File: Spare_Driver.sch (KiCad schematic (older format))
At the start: 48 parts, among them J12 CHECK FOOTPRINT, J13 CHECK FOOTPRINT, J14 Conn_01x02_Male, J15 Conn_01x02_Male, U10 TMC2130-LA, U9 TMC2130-LA

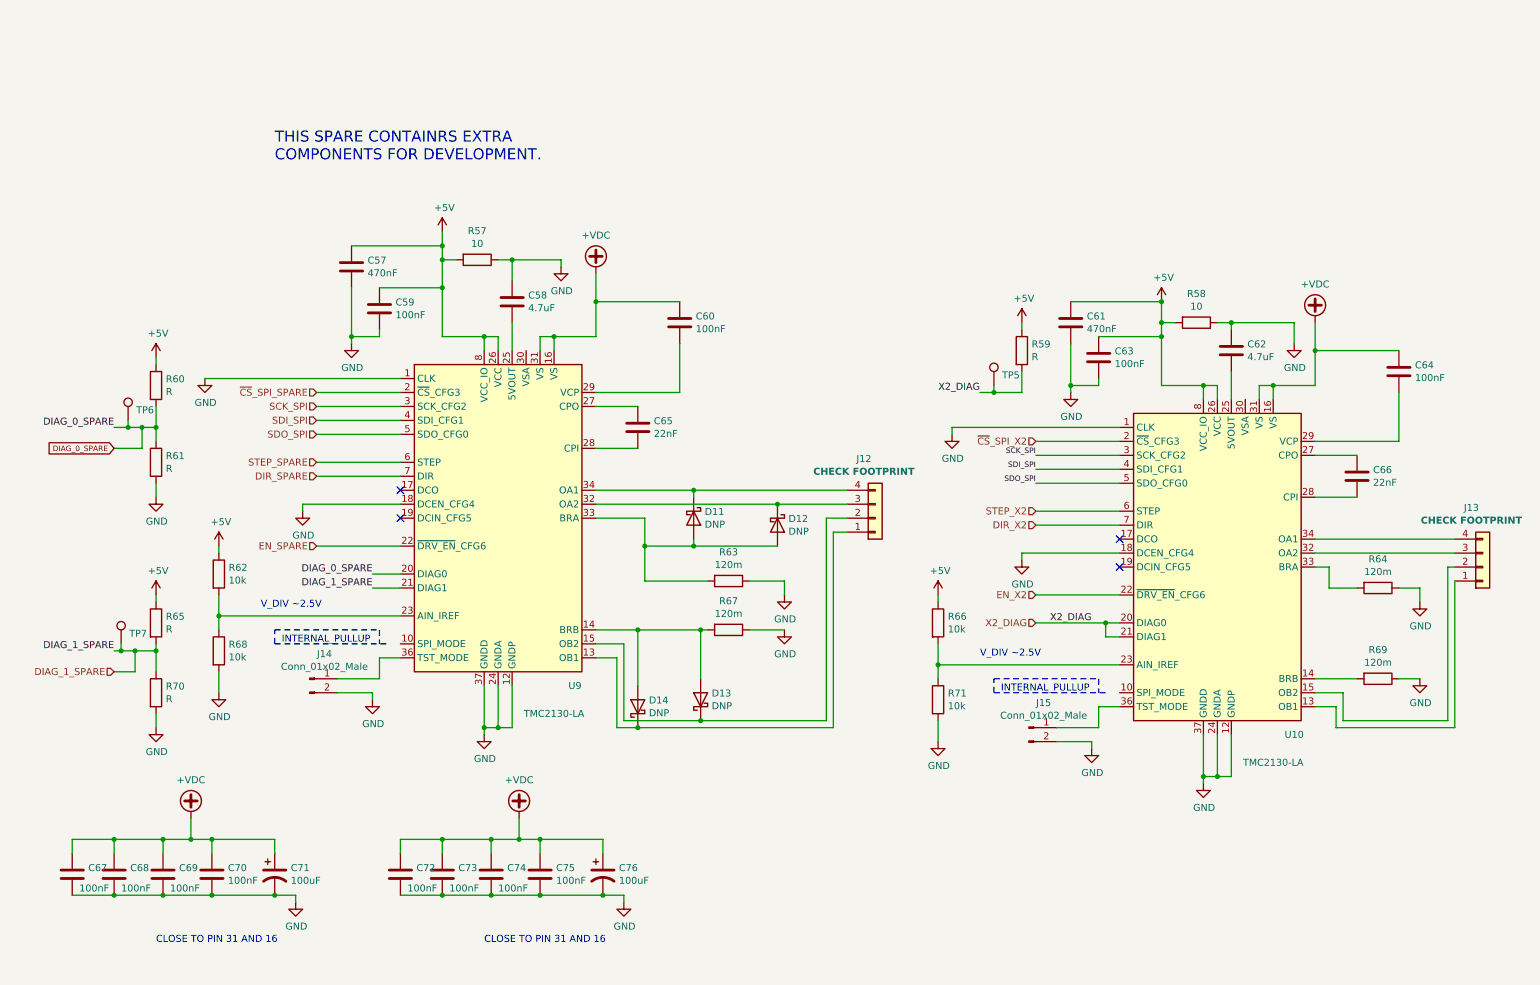
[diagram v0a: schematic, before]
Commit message: Fixed X,Y,Z driver bus connection. set up spare and X2
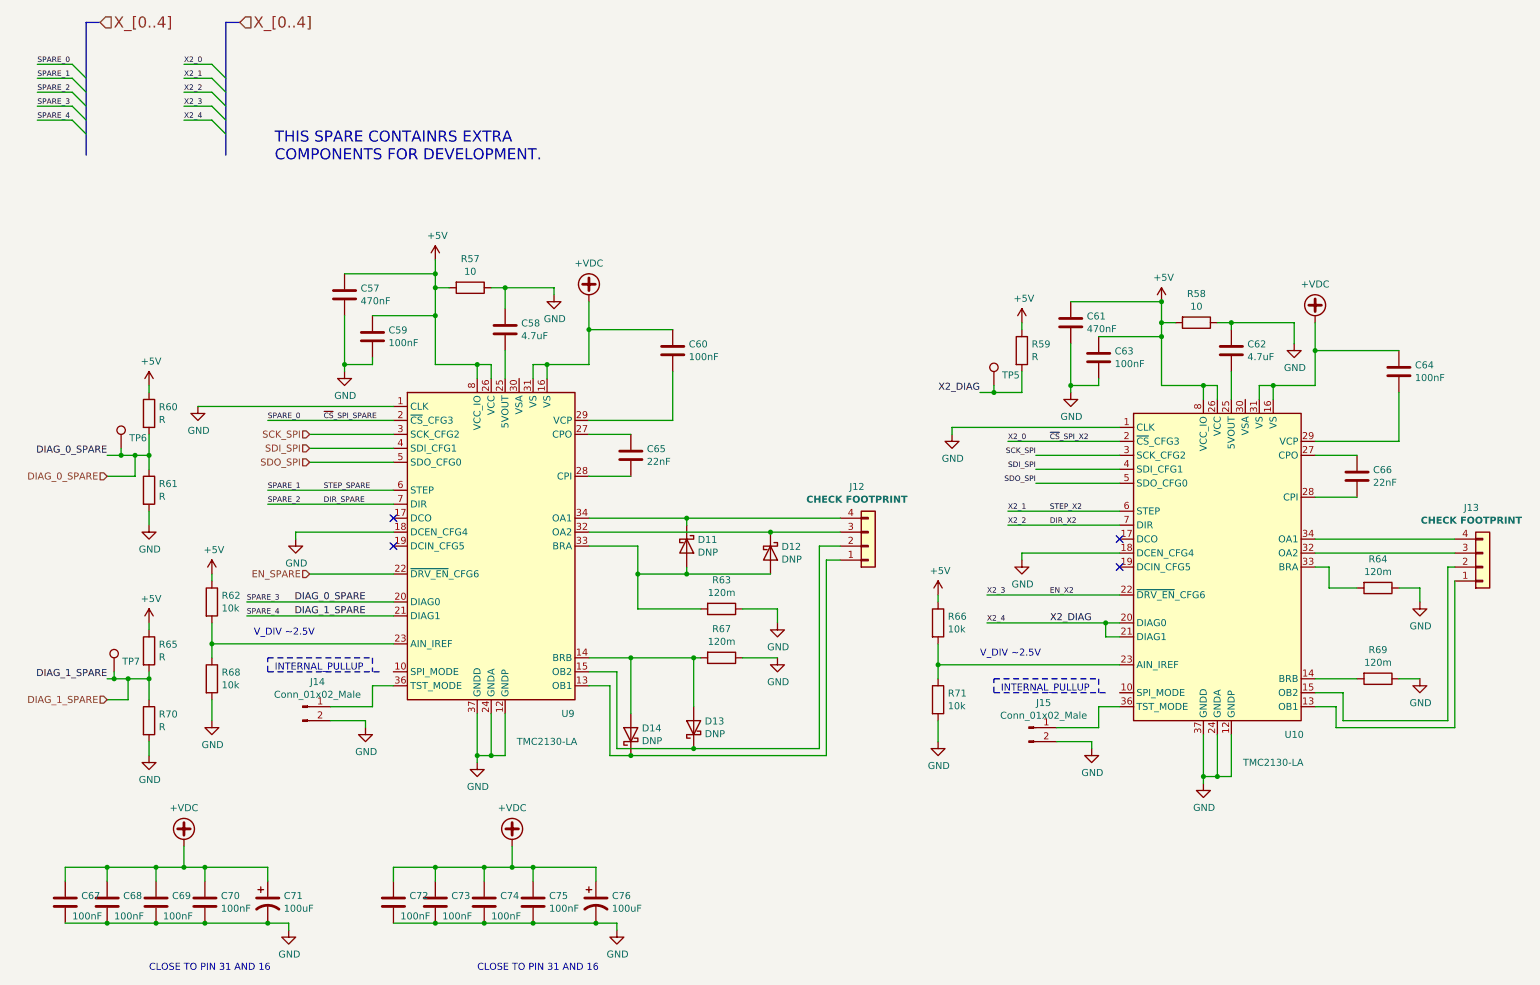
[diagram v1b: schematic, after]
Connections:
- net STEP_SPARE renamed SPARE_1
- net X2_DIAG renamed X2_4
- net ~CS~_SPI_SPARE renamed SPARE_0
- net ~CS~_SPI_X2 renamed X2_0
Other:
- moved on the sheet: C57, C58, C59, C60, C65, C67, C68, C69, C70, C71, C72, C73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

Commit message: added peripherals
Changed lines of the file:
@@
 Wire Wire Line
 	1800 1050 1600 1050
-Wire Bus Line
-	900  750  900  1700
-Wire Bus Line
-	1900 750  1900 1700
 Wire Wire Line
 	1800 1150 1600 1150
@@
 Text Label 1600 1450 0    39   ~ 0
 X2_4
+Wire Wire Line
+	7500 1050 7750 1050
+Wire Wire Line
+	7500 1150 7750 1150
+Wire Wire Line
+	7500 1250 7750 1250
+Wire Wire Line
+	7500 1350 7750 1350
+Wire Wire Line
+	7500 1450 7750 1450
+Entry Wire Line
+	7750 1050 7850 1150
+Entry Wire Line
+	7750 1150 7850 1250
+Entry Wire Line
+	7750 1250 7850 1350
+Entry Wire Line
+	7750 1350 7850 1450
+Entry Wire Line
+	7750 1450 7850 1550
+Text HLabel 7950 750  2    79   Input ~ 0
+X2_[0..4]
+Wire Bus Line
+	7850 750  7950 750
+Text Label 7500 1050 0    59   ~ 0
+X2_0
+Text Label 7500 1150 0    59   ~ 0
+X2_1
+Text Label 7500 1250 0    59   ~ 0
+X2_2
+Text Label 7500 1350 0    59   ~ 0
+X2_3
+Text Label 7500 1450 0    59   ~ 0
+X2_4
+Wire Bus Line
+	900  750  900  1700
+Wire Bus Line
+	1900 750  1900 1700
+Wire Bus Line
+	7850 750  7850 1700
 $EndSCHEMATC

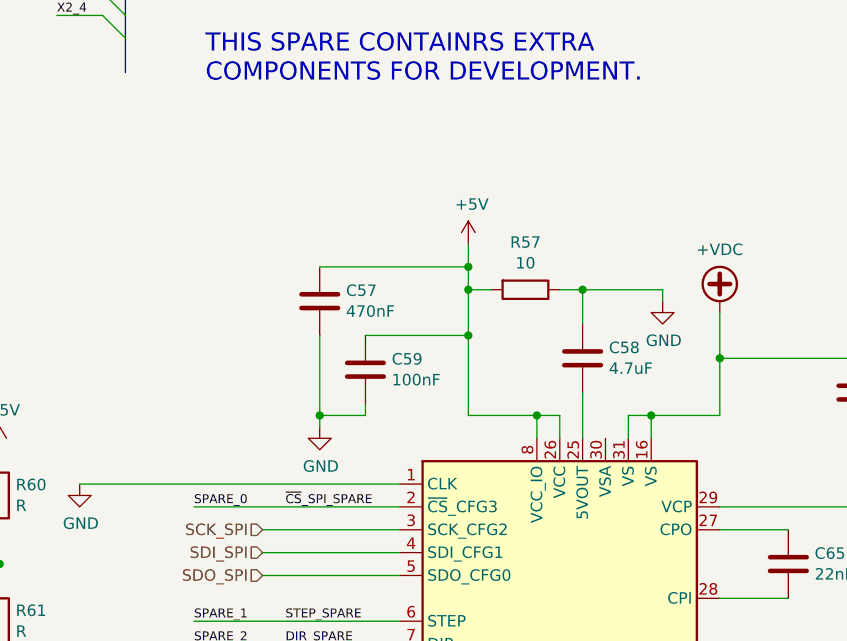
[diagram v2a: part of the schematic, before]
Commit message: Found error in stepper driver supply
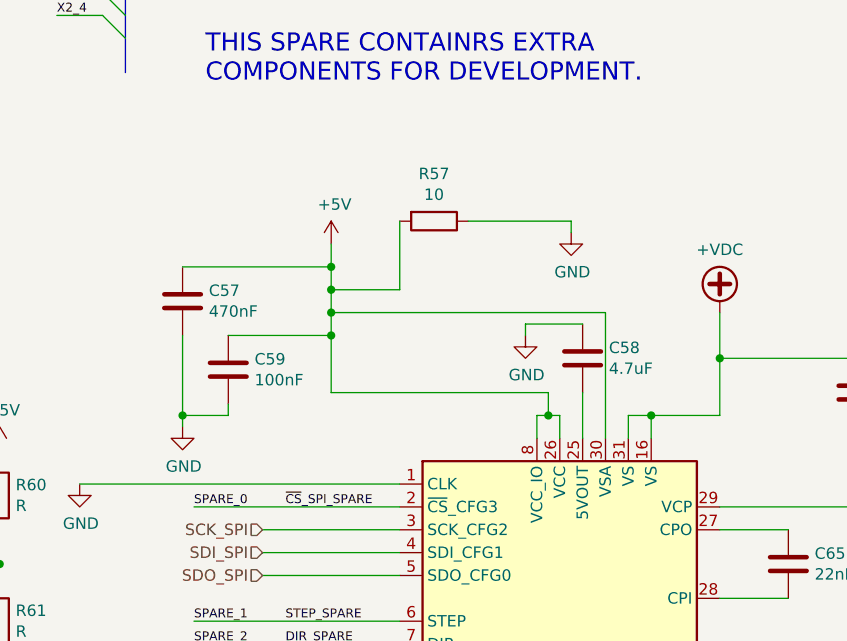
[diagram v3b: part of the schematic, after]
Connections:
- net +5V: now also U9.30 (VSA)
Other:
- moved on the sheet: C57, C59, R57
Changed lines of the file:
@@
 EESchema Schematic File Version 4
-LIBS:bountifulHarvest-cache
-EELAYER 26 0
+EELAYER 30 0
 EELAYER END
 $Descr A4 11693 8268
@@
 L power:+5V #PWR0182
 U 1 1 5EF23B3D
-P 3400 2450
-F 0 "#PWR0182" H 3400 2300 50  0001 C CNN
-F 1 "+5V" H 3415 2623 50  0000 C CNN
-F 2 "" H 3400 2450 50  0001 C CNN
-F 3 "" H 3400 2450 50  0001 C CNN
-	1    3400 2450
+P 2800 2450
+F 0 "#PWR0182" H 2800 2300 50  0001 C CNN
+F 1 "+5V" H 2815 2623 50  0000 C CNN
+F 2 "" H 2800 2450 50  0001 C CNN
+F 3 "" H 2800 2450 50  0001 C CNN
+	1    2800 2450
 	1    0    0    -1
 $EndComp
@@
 L Device:C C57
 U 1 1 5EF25811
-P 2750 2700
-F 0 "C57" H 2865 2746 50  0000 L CNN
-F 1 "470nF" H 2865 2655 50  0000 L CNN
-F 2 "" H 2788 2550 50  0001 C CNN
-F 3 "~" H 2750 2700 50  0001 C CNN
-F 4 "GCM21BR71H474KA55L" H 2750 2700 50  0001 C CNN "Manufacturer P/N"
-F 5 "Digi-Key" H 2750 2700 50  0001 C CNN "Vendor"
-F 6 "490-4788-1-ND" H 2750 2700 50  0001 C CNN "Vendor P/N"
-	1    2750 2700
+P 2150 2700
+F 0 "C57" H 2265 2746 50  0000 L CNN
+F 1 "470nF" H 2265 2655 50  0000 L CNN
+F 2 "" H 2188 2550 50  0001 C CNN
+F 3 "~" H 2150 2700 50  0001 C CNN
+F 4 "GCM21BR71H474KA55L" H 2150 2700 50  0001 C CNN "Manufacturer P/N"
+F 5 "Digi-Key" H 2150 2700 50  0001 C CNN "Vendor"
+F 6 "490-4788-1-ND" H 2150 2700 50  0001 C CNN "Vendor P/N"
+	1    2150 2700
 	1    0    0    -1
 $EndComp
@@
 L power:GND #PWR0183
 U 1 1 5FBEF509
-P 2750 3250
-F 0 "#PWR0183" H 2750 3000 50  0001 C CNN
-F 1 "GND" H 2755 3077 50  0000 C CNN
-F 2 "" H 2750 3250 50  0001 C CNN
-F 3 "" H 2750 3250 50  0001 C CNN
-	1    2750 3250
-	1    0    0    -1
-$EndComp
-Wire Wire Line
-	2750 2850 2750 3200
+P 2150 3250
+F 0 "#PWR0183" H 2150 3000 50  0001 C CNN
+F 1 "GND" H 2155 3077 50  0000 C CNN
+F 2 "" H 2150 3250 50  0001 C CNN
+F 3 "" H 2150 3250 50  0001 C CNN
+	1    2150 3250
+	1    0    0    -1
+$EndComp
+Wire Wire Line
+	2150 2850 2150 3200
 $Comp
 L power:GND #PWR0184
@@
 Wire Wire Line
 	3700 3300 3700 3200
-Wire Wire Line
-	3700 3200 3400 3200
 $Comp
 L Device:C C58
@@
 Wire Wire Line
 	5100 3250 5100 3600
-Wire Wire Line
-	3900 2800 3900 2650
-Connection ~ 3700 3200
-Wire Wire Line
-	3700 3200 3800 3200
 Wire Wire Line
 	1400 7200 1750 7200
@@
 L power:GND #PWR0199
 U 1 1 5FFA5DDD
-P 4250 2700
-F 0 "#PWR0199" H 4250 2450 50  0001 C CNN
-F 1 "GND" H 4255 2527 50  0000 C CNN
-F 2 "" H 4250 2700 50  0001 C CNN
-F 3 "" H 4250 2700 50  0001 C CNN
-	1    4250 2700
-	1    0    0    -1
-$EndComp
-Wire Wire Line
-	4250 2650 4250 2700
-Wire Wire Line
-	4250 2650 3900 2650
+P 3850 2400
+F 0 "#PWR0199" H 3850 2150 50  0001 C CNN
+F 1 "GND" H 3855 2227 50  0000 C CNN
+F 2 "" H 3850 2400 50  0001 C CNN
+F 3 "" H 3850 2400 50  0001 C CNN
+	1    3850 2400
+	1    0    0    -1
+$EndComp
+Wire Wire Line
+	3850 2350 3850 2400
 $Comp
 L Device:R R57
 U 1 1 5FFAEB96
-P 3650 2650
-F 0 "R57" V 3443 2650 50  0000 C CNN
-F 1 "10" V 3534 2650 50  0000 C CNN
-F 2 "" V 3580 2650 50  0001 C CNN
-F 3 "~" H 3650 2650 50  0001 C CNN
-F 4 "Digi-Key" H 3650 2650 50  0001 C CNN "Vendor"
-F 5 "13-RE0805FRE0710RLCT-ND" H 3650 2650 50  0001 C CNN "Vendor P/N"
-	1    3650 2650
+P 3250 2350
+F 0 "R57" V 3043 2350 50  0000 C CNN
+F 1 "10" V 3134 2350 50  0000 C CNN
+F 2 "" V 3180 2350 50  0001 C CNN
+F 3 "~" H 3250 2350 50  0001 C CNN
+F 4 "Digi-Key" H 3250 2350 50  0001 C CNN "Vendor"
+F 5 "13-RE0805FRE0710RLCT-ND" H 3250 2350 50  0001 C CNN "Vendor P/N"
+	1    3250 2350
 	0    1    1    0
 $EndComp
-Wire Wire Line
-	3900 2650 3800 2650
-Connection ~ 3900 2650
-Wire Wire Line
-	3500 2650 3400 2650
-Connection ~ 3400 2650
-Wire Wire Line
-	3400 2650 3400 2850
+Connection ~ 2800 2650
 $Comp
 L Device:C C59
 U 1 1 5FFB4F6A
-P 2950 3000
-F 0 "C59" H 3065 3046 50  0000 L CNN
-F 1 "100nF" H 3065 2955 50  0000 L CNN
-F 2 "Capacitors_SMD:C_0805_HandSoldering" H 2988 2850 50  0001 C CNN
-F 3 "~" H 2950 3000 50  0001 C CNN
-F 4 "Digi-Key" H 2950 3000 50  0001 C CNN "Vendor"
-F 5 "1276-6557-1-ND" H 2950 3000 50  0001 C CNN "Vendor P/N"
-	1    2950 3000
-	1    0    0    -1
-$EndComp
-Connection ~ 3400 2850
-Wire Wire Line
-	3400 2850 3400 3200
-Wire Wire Line
-	2950 3150 2950 3200
-Wire Wire Line
-	2950 3200 2750 3200
-Connection ~ 2750 3200
-Wire Wire Line
-	2750 3200 2750 3250
+P 2350 3000
+F 0 "C59" H 2465 3046 50  0000 L CNN
+F 1 "100nF" H 2465 2955 50  0000 L CNN
+F 2 "Capacitors_SMD:C_0805_HandSoldering" H 2388 2850 50  0001 C CNN
+F 3 "~" H 2350 3000 50  0001 C CNN
+F 4 "Digi-Key" H 2350 3000 50  0001 C CNN "Vendor"
+F 5 "1276-6557-1-ND" H 2350 3000 50  0001 C CNN "Vendor P/N"
+	1    2350 3000
+	1    0    0    -1
+$EndComp
+Wire Wire Line
+	2350 3150 2350 3200
+Wire Wire Line
+	2350 3200 2150 3200
+Connection ~ 2150 3200
+Wire Wire Line
+	2150 3200 2150 3250
 $Comp
 L Device:R R61
@@
 	1050 7200 1400 7200
 Wire Wire Line
-	3400 2450 3400 2550
-Wire Wire Line
-	2950 2850 3400 2850
-Wire Wire Line
-	2750 2550 3400 2550
-Connection ~ 3400 2550
-Wire Wire Line
-	3400 2550 3400 2650
+	2350 2850 2800 2850
+Wire Wire Line
+	2150 2550 2800 2550
 Wire Wire Line
 	1700 3500 3100 3500
@@
 Text Label 7500 1450 0    59   ~ 0
 X2_4
+Wire Wire Line
+	2800 2650 2800 2750
+Wire Wire Line
+	2800 2450 2800 2550
+Connection ~ 2800 2550
+Wire Wire Line
+	2800 2550 2800 2650
+Connection ~ 2800 2850
+Wire Wire Line
+	3400 2350 3850 2350
+Wire Wire Line
+	3100 2650 3100 2350
+Wire Wire Line
+	2800 2650 3100 2650
+Wire Wire Line
+	4000 3300 4000 2750
+Wire Wire Line
+	4000 2750 2800 2750
+Connection ~ 2800 2750
+Wire Wire Line
+	2800 2750 2800 2850
+$Comp
+L power:GND #PWR?
+U 1 1 61DABB29
+P 3650 2850
+F 0 "#PWR?" H 3650 2600 50  0001 C CNN
+F 1 "GND" H 3655 2677 50  0000 C CNN
+F 2 "" H 3650 2850 50  0001 C CNN
+F 3 "" H 3650 2850 50  0001 C CNN
+	1    3650 2850
+	1    0    0    -1
+$EndComp
+Wire Wire Line
+	3900 2800 3650 2800
+Wire Wire Line
+	3650 2800 3650 2850
+Wire Wire Line
+	2800 2850 2800 3100
+Wire Wire Line
+	3700 3200 3750 3200
+Wire Wire Line
+	2800 3100 3750 3100
+Wire Wire Line
+	3750 3100 3750 3200
+Connection ~ 3750 3200
+Wire Wire Line
+	3750 3200 3800 3200
 Wire Bus Line
 	900  750  900  1700

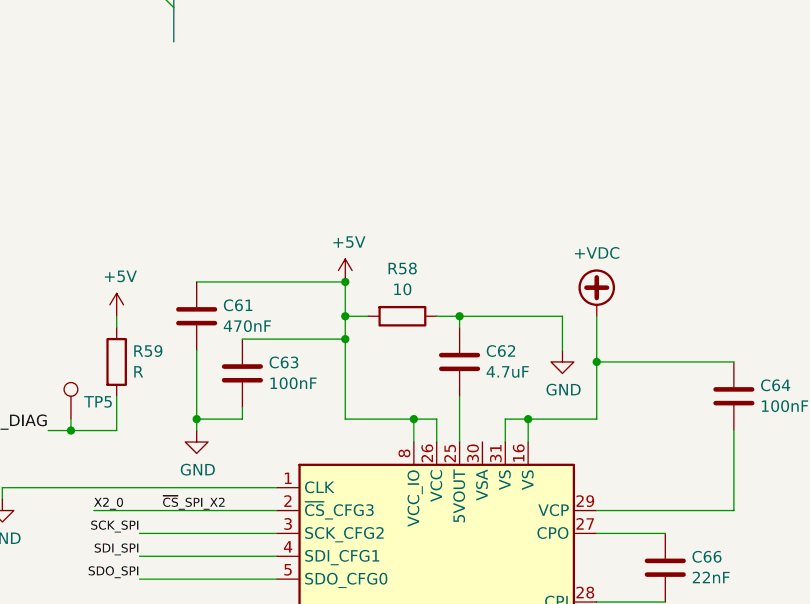
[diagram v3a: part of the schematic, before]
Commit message: updated ATMEGA and regulators
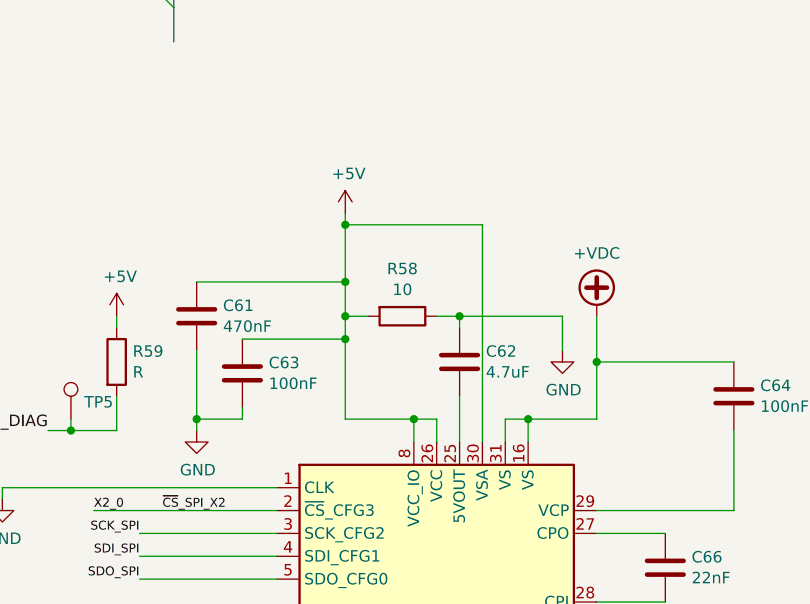
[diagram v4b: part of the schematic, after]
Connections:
- net +5V: now also U10.30 (VSA)
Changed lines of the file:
@@
 L power:+5V #PWR0200
 U 1 1 6026AD4B
-P 8600 2750
+P 8600 2450
 AR Path="/5EEE69C6/6026AD4B" Ref="#PWR0200"  Part="1"
 AR Path="/5FF92876/6026AD4B" Ref="#PWR?"  Part="1"
-F 0 "#PWR0200" H 8600 2600 50  0001 C CNN
-F 1 "+5V" H 8615 2923 50  0000 C CNN
-F 2 "" H 8600 2750 50  0001 C CNN
-F 3 "" H 8600 2750 50  0001 C CNN
-	1    8600 2750
+F 0 "#PWR0200" H 8600 2300 50  0001 C CNN
+F 1 "+5V" H 8615 2623 50  0000 C CNN
+F 2 "" H 8600 2450 50  0001 C CNN
+F 3 "" H 8600 2450 50  0001 C CNN
+	1    8600 2450
 	1    0    0    -1
 $EndComp
@@
 Wire Wire Line
 	3750 3200 3800 3200
+Wire Wire Line
+	8600 2450 8600 2500
+Wire Wire Line
+	8600 2500 9200 2500
+Wire Wire Line
+	9200 2500 9200 3450
+Connection ~ 8600 2500
+Wire Wire Line
+	8600 2500 8600 2750
 Wire Bus Line
 	900  750  900  1700

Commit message: added footprints for most of the c,r, and tp's. need new buck
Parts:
- R57, R58: footprint (none) -> Resistors_SMD:R_0603_HandSoldering
- TP5, TP6, TP7: footprint Measurement_Points:Test_Point_Keystone_5000-5004_Miniature -> Measurement_Points:Test_Point_Keystone_5015_Micro-Minature
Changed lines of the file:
@@
 EESchema Schematic File Version 4
-EELAYER 30 0
+LIBS:bountifulHarvest-cache
+EELAYER 26 0
 EELAYER END
 $Descr A4 11693 8268
@@
 F 0 "TP6" H 1208 3874 50  0000 L CNN
 F 1 "TestPoint" H 1208 3829 50  0001 L CNN
-F 2 "Measurement_Points:Test_Point_Keystone_5000-5004_Miniature" H 1350 3800 50  0001 C CNN
+F 2 "Measurement_Points:Test_Point_Keystone_5015_Micro-Minature" H 1350 3800 50  0001 C CNN
 F 3 "~" H 1350 3800 50  0001 C CNN
 	1    1150 3800
@@
 F 0 "TP7" H 1158 5474 50  0000 L CNN
 F 1 "TestPoint" H 1158 5429 50  0001 L CNN
-F 2 "Measurement_Points:Test_Point_Keystone_5000-5004_Miniature" H 1300 5400 50  0001 C CNN
+F 2 "Measurement_Points:Test_Point_Keystone_5015_Micro-Minature" H 1300 5400 50  0001 C CNN
 F 3 "~" H 1300 5400 50  0001 C CNN
 	1    1100 5400
@@
 F 0 "R57" V 3043 2350 50  0000 C CNN
 F 1 "10" V 3134 2350 50  0000 C CNN
-F 2 "" V 3180 2350 50  0001 C CNN
+F 2 "Resistors_SMD:R_0603_HandSoldering" V 3180 2350 50  0001 C CNN
 F 3 "~" H 3250 2350 50  0001 C CNN
 F 4 "Digi-Key" H 3250 2350 50  0001 C CNN "Vendor"
@@
 F 0 "TP5" H 7458 3424 50  0000 L CNN
 F 1 "TestPoint" H 7458 3379 50  0001 L CNN
-F 2 "Measurement_Points:Test_Point_Keystone_5000-5004_Miniature" H 7600 3350 50  0001 C CNN
+F 2 "Measurement_Points:Test_Point_Keystone_5015_Micro-Minature" H 7600 3350 50  0001 C CNN
 F 3 "~" H 7600 3350 50  0001 C CNN
 	1    7400 3350
@@
 F 0 "R58" V 8643 2900 50  0000 C CNN
 F 1 "10" V 8734 2900 50  0000 C CNN
-F 2 "" V 8780 2900 50  0001 C CNN
+F 2 "Resistors_SMD:R_0603_HandSoldering" V 8780 2900 50  0001 C CNN
 F 3 "~" H 8850 2900 50  0001 C CNN
 F 4 "Digi-Key" H 8850 2900 50  0001 C CNN "Vendor"
